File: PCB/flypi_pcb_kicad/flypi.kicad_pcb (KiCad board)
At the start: 2 copper layers, 76.1 x 85.1 mm, 45 parts, among them CON1 BARREL_JACK, J12 USB_A, P1 PeltS1S2, P10 RGB GB-R, P3 Fan-+, P4 Therm -s+, P5 HP1+-, P6 HP2-+, P7 servo -s+, P8 Ring s-+, P9 I2C +-scsd, Q1 1A_NPN_EBC, Q2 1A-NPN-EBC, Q3 1A_NPN_EBC, Q4 1A_NPN_EBC, U1 LM2596, U2 LM2596, U4 L298N, U5 arduino_mini

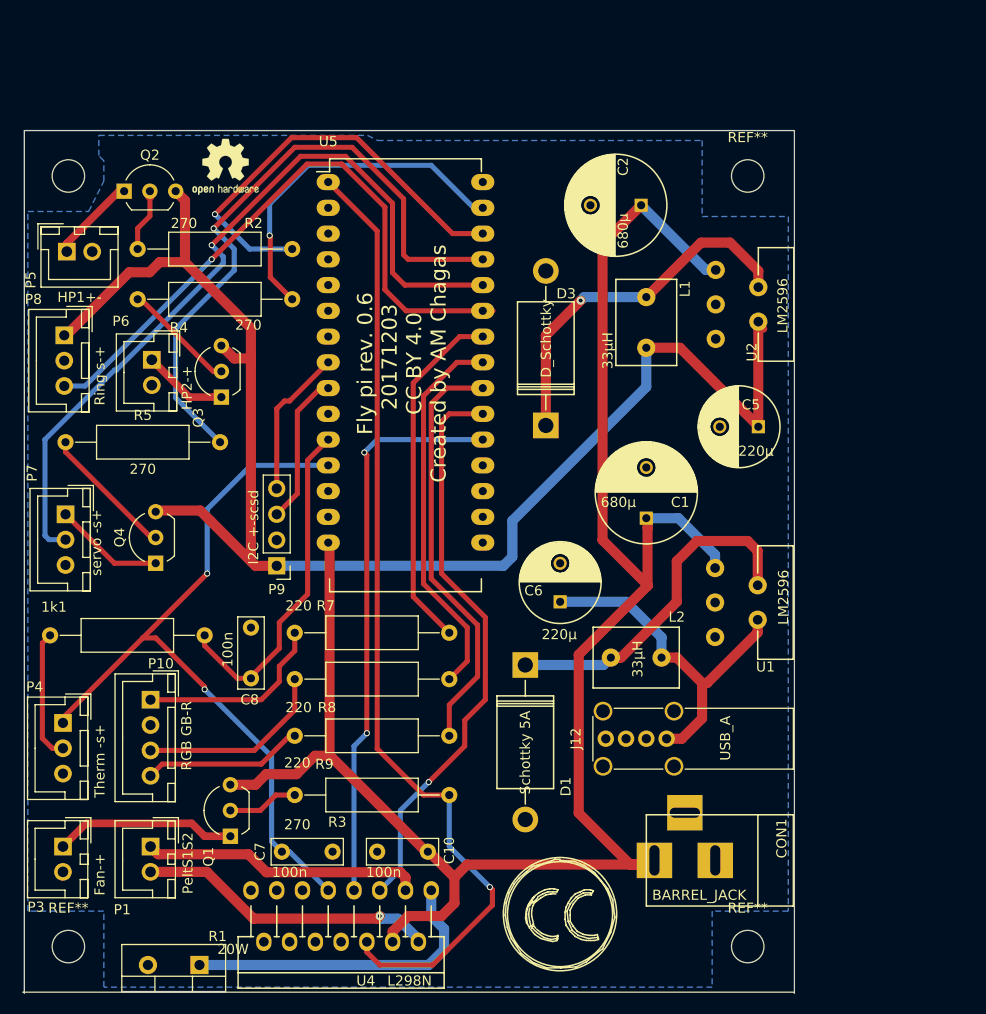
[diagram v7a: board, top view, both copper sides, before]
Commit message: found bug in gerbers
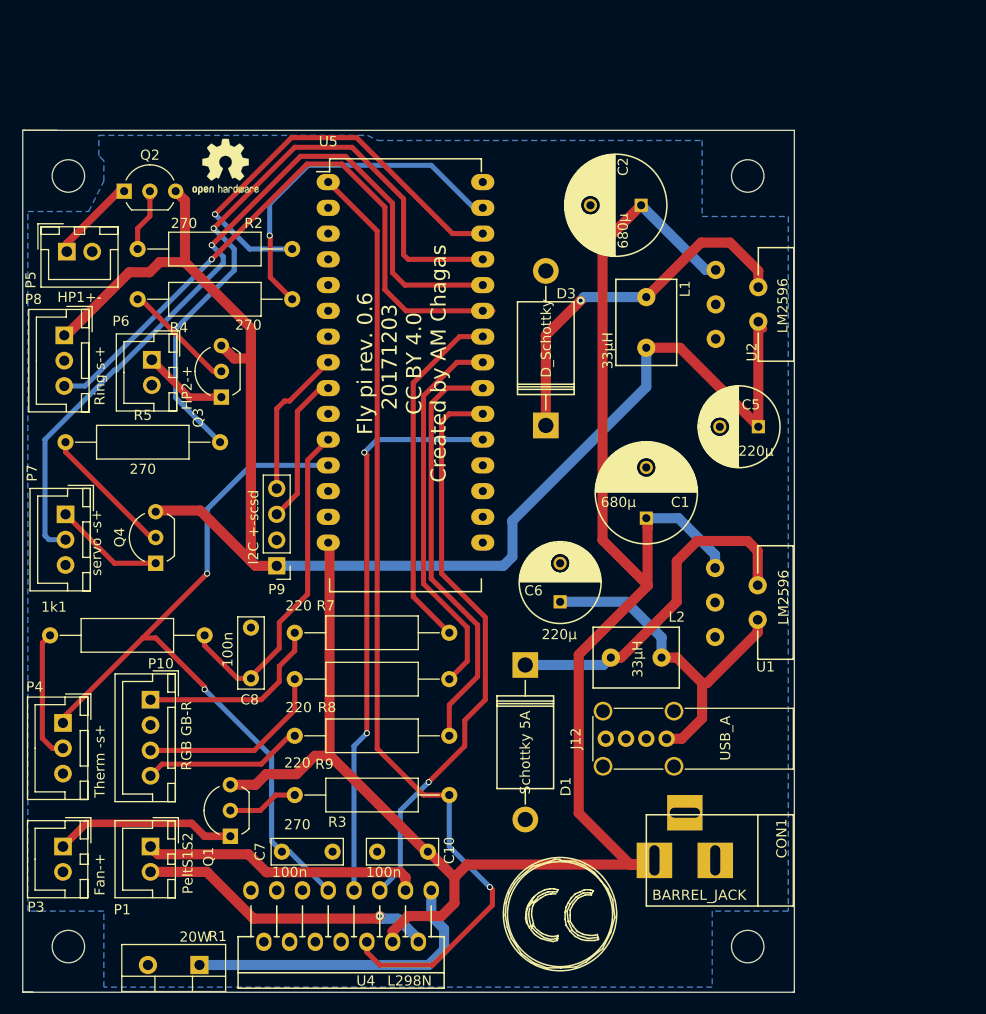
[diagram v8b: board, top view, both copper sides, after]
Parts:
- ? (x3): renamed from REF**; value MountingHole_3.2mm_M3_DIN965 -> (none)
- ?: renamed from REF***; value OSHW-Logo2_7.3x6mm_SilkScreen -> (none)
- ?: value Symbol_CreativeCommons_SilkScreenTop_Type2_Big -> (none)
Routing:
- net (no net): track 0.51 -> 0.00 mm
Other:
- board size 76.1 x 85.1 mm -> 76.1 x 85 mm
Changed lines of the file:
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@@
     (area 68.750001 33.044987 212.785715 161.577001)
     (thickness 1.6)
-    (drawings 30)
-    (tracks 301)
+    (drawings 37)
+    (tracks 300)
     (zones 0)
     (modules 45)
@@
     (41 Cmts.User user)
     (42 Eco1.User user)
-    (43 Eco2.User user)
+    (43 Eco2.User user hide)
     (44 Edge.Cuts user)
     (45 Margin user)
@@
     (pad_drill 0.6)
     (pad_to_mask_clearance 0)
-    (aux_axis_origin 105.156 134.112)
+    (aux_axis_origin 105 134)
     (visible_elements 7FFFFFFF)
     (pcbplotparams
@@
       (effects (font (size 1 1) (thickness 0.15)))
     )
-    (fp_text value "20W " (at -3.312 1.554 180) (layer F.SilkS)
-      (effects (font (size 1 1) (thickness 0.15)))
-    )
-    (fp_text user %R (at 2.54 -3.62 180) (layer F.Fab)
+    (fp_text value "20W " (at 0.428 2.768 180) (layer F.SilkS)
+      (effects (font (size 1 1) (thickness 0.15)))
+    )
+    (fp_text user %R (at -1.822 2.868 180) (layer F.Fab)
       (effects (font (size 1 1) (thickness 0.15)))
     )
@@
     (tags "mounting hole 3.2mm no annular m3 din965")
     (attr virtual)
-    (fp_text reference REF** (at 0 -3.8) (layer F.SilkS)
-      (effects (font (size 1 1) (thickness 0.15)))
-    )
-    (fp_text value MountingHole_3.2mm_M3_DIN965 (at 0 7.62) (layer F.Fab)
+    (fp_text reference "" (at 0 -3.8) (layer F.SilkS)
+      (effects (font (size 1 1) (thickness 0.15)))
+    )
+    (fp_text value "" (at 0.3 6.9) (layer F.Fab)
       (effects (font (size 1 1) (thickness 0.15)))
     )
@@
     (tags "mounting hole 3.2mm no annular m3 din965")
     (attr virtual)
-    (fp_text reference REF** (at 0 -3.8) (layer F.SilkS)
-      (effects (font (size 1 1) (thickness 0.15)))
-    )
-    (fp_text value MountingHole_3.2mm_M3_DIN965 (at 0 3.8) (layer F.Fab)
+    (fp_text reference "" (at 0 -3.8) (layer F.SilkS)
+      (effects (font (size 1 1) (thickness 0.15)))
+    )
+    (fp_text value "" (at 0 3.8) (layer F.Fab)
       (effects (font (size 1 1) (thickness 0.15)))
     )
@@
     (tags "Logo Symbol OSHW")
     (attr virtual)
-    (fp_text reference REF*** (at 0 0) (layer F.SilkS) hide
-      (effects (font (size 1 1) (thickness 0.15)))
-    )
-    (fp_text value OSHW-Logo2_7.3x6mm_SilkScreen (at 2.032 1.27) (layer F.Fab) hide
+    (fp_text reference "" (at 0 0) (layer F.SilkS) hide
+      (effects (font (size 1 1) (thickness 0.15)))
+    )
+    (fp_text value "" (at 2.032 1.27) (layer F.Fab) hide
       (effects (font (size 1 1) (thickness 0.15)))
     )
@@
       (effects (font (size 1 1) (thickness 0.15)))
     )
-    (fp_text value Symbol_CreativeCommons_SilkScreenTop_Type2_Big (at 0.59944 8.001) (layer F.Fab) hide
+    (fp_text value "" (at 0.59944 8.001) (layer Eco2.User) hide
       (effects (font (size 1 1) (thickness 0.15)))
     )
@@
     (tags "mounting hole 3.2mm no annular m3 din965")
     (attr virtual)
-    (fp_text reference REF** (at 0 -3.8) (layer F.SilkS)
-      (effects (font (size 1 1) (thickness 0.15)))
-    )
-    (fp_text value MountingHole_3.2mm_M3_DIN965 (at 0 3.8) (layer F.Fab)
-      (effects (font (size 1 1) (thickness 0.15)))
-    )
-    (fp_text user %R (at 0.3 0) (layer F.Fab)
+    (fp_text reference "" (at 0 -3.8) (layer F.SilkS)
+      (effects (font (size 1 1) (thickness 0.15)))
+    )
+    (fp_text value "" (at 0 3.8) (layer F.Fab)
+      (effects (font (size 1 1) (thickness 0.15)))
+    )
+    (fp_text user "" (at 0.3 0) (layer F.Fab)
       (effects (font (size 1 1) (thickness 0.15)))
     )
@@
     (pad 1 np_thru_hole circle (at 0 0) (size 3.2 3.2) (drill 3.2) (layers *.Cu *.Mask))
   )
+  (gr_line (start 105 49) (end 105 134) (angle 90) (layer Edge.Cuts) (width 0.1))
+  (gr_line (start 181.1 49) (end 105 49) (angle 90) (layer Edge.Cuts) (width 0.1))
+  (gr_line (start 181.1 134) (end 181.1 49) (angle 90) (layer Edge.Cuts) (width 0.1))
+  (gr_line (start 105 134) (end 181.1 134) (angle 90) (layer Edge.Cuts) (width 0.1))
+  (target plus (at 105 134) (size 5) (width 0.1) (layer Edge.Cuts))
+  (target plus (at 105 49) (size 5) (width 0.1) (layer Edge.Cuts))
+  (target plus (at 181.1 49) (size 5) (width 0.1) (layer Edge.Cuts))
+  (gr_line (start 106 134) (end 105 134) (angle 90) (layer Edge.Cuts) (width 0.1))
+  (target plus (at 181.1 134) (size 5) (width 0.1) (layer Edge.Cuts))
+  (gr_line (start 105.15 49) (end 108.4 49) (angle 90) (layer Edge.Cuts) (width 0.1))
+  (gr_line (start 105.15 49) (end 105 49) (angle 90) (layer Edge.Cuts) (width 0.1))
+  (gr_line (start 181.05 134) (end 181.1 134) (angle 90) (layer Edge.Cuts) (width 0.1))
+  (gr_line (start 181 134) (end 181.1 134) (angle 90) (layer Edge.Cuts) (width 0.1))
   (dimension 28.570112 (width 0.3) (layer Eco2.User)
     (gr_text "28,570 mm" (at 119.473509 42.818728 359.8395642) (layer Eco2.User)
@@
     (arrow2b (pts (xy 188.468 134.112) (xy 187.881579 132.985496)))
   )
-  (gr_line (start 105.156 49.022) (end 105.156 134.112) (angle 90) (layer Edge.Cuts) (width 0.1))
-  (gr_line (start 181.102 49.022) (end 181.102 134.112) (angle 90) (layer Edge.Cuts) (width 0.1))
-  (gr_line (start 105.156 49.022) (end 181.102 49.022) (angle 90) (layer Edge.Cuts) (width 0.1))
-  (gr_text "www.prometheus-science.com\nhttps://github.com/prometheus-science/Flypi" (at 125.222 77.724 270) (layer B.SilkS)
+  (gr_text "www.prometheus-science.com\nhttps://github.com/prometheus-science/Flypi" (at 141 79 270) (layer B.SilkS)
     (effects (font (size 1.5 1.5) (thickness 0.3)) (justify mirror))
   )
-  (dimension 38.020084 (width 0.3) (layer B.CrtYd)
-    (gr_text "38,020 mm" (at 123.968669 34.544987 0.1205590636) (layer B.CrtYd)
+  (dimension 38.020084 (width 0.3) (layer Eco2.User)
+    (gr_text "38,020 mm" (at 123.968669 34.544987 0.1205590636) (layer Eco2.User)
       (effects (font (size 1.5 1.5) (thickness 0.3)))
     )
@@
     (arrow2b (pts (xy 104.96151 35.934984) (xy 106.086777 35.346194)))
   )
-  (target plus (at 105.156 134.112) (size 5) (width 0.1) (layer Edge.Cuts))
-  (target plus (at 181.05 134.05) (size 5) (width 0.1) (layer Edge.Cuts))
   (gr_text "Fly pi rev. 0.6\n  20171203\nCC BY 4.0\nCreated by AM Chagas\n\n" (at 143.6 72 90) (layer F.SilkS)
     (effects (font (size 1.5 1.5) (thickness 0.3)))
   )
-  (gr_line (start 181 134) (end 105 134) (angle 90) (layer Edge.Cuts) (width 0.1))
-  (segment (start 177.292 129.54) (end 177.292 130.048) (width 1) (layer F.Cu) (net 0) (status 30))
   (segment (start 127.508 103.044) (end 127.508 102.87) (width 0.5) (layer F.Cu) (net 1) (status 30))
   (segment (start 127.508 102.87) (end 130.302 100.076) (width 0.5) (layer F.Cu) (net 1) (status 10))
